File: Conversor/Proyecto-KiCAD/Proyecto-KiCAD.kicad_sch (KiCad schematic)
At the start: 6 parts

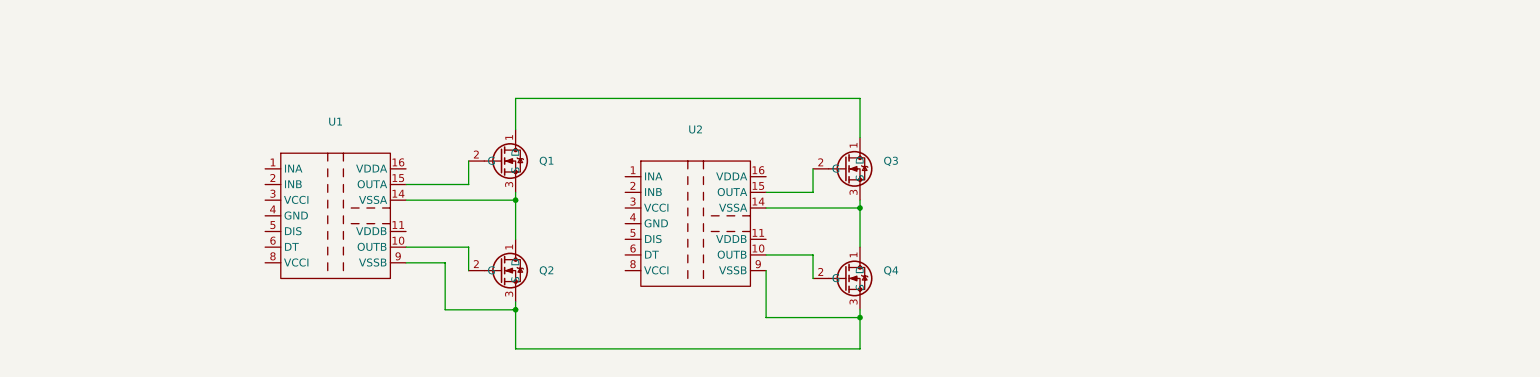
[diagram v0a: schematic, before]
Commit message: Comenzar el diseño de la plaqueta en KiCAD
- Empece a ver el diseño de los drivers para los MOSFETs
- Agregue la datasheet de la fuente aislada TRACO
- Hay que leer la nota de aplicacion para el diseño del circuito de bootstrap a la salida y elegir Cboot, Rboot y Dboot
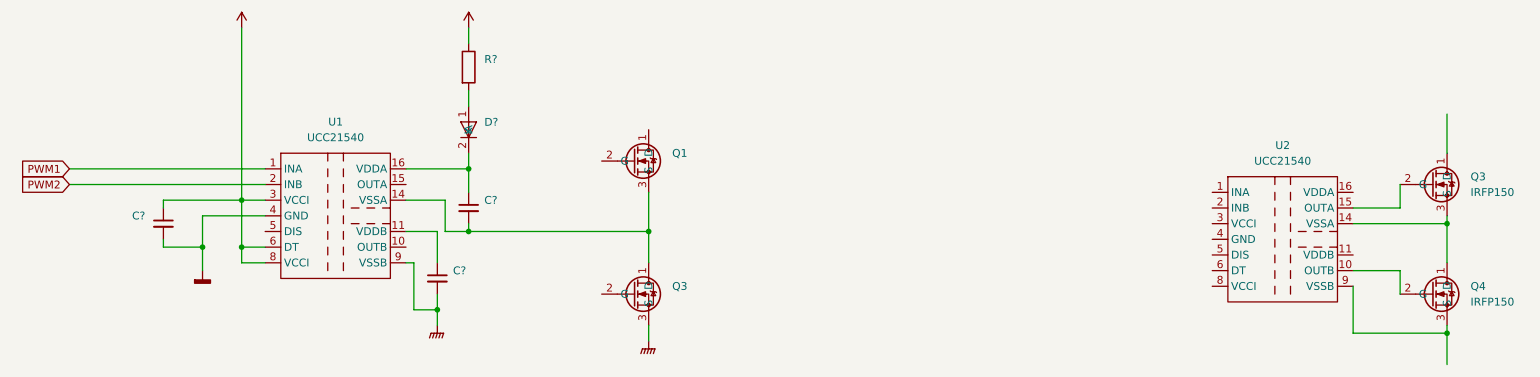
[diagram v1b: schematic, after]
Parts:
- removed Q2: (no value), symbol Componentes proyecto:IRFP150
- added C? (x3): (no value), symbol Device:C_Small
- added D?: (no value), symbol Componentes proyecto:MUR160
- added Q3: (no value), symbol Componentes proyecto:IRFP150
- added R?: (no value), symbol Device:R
- Q3, Q4: value (none) -> IRFP150; footprint (none) -> Package_TO_SOT_THT:TO-247-3_Horizontal_TabDown
- U1, U2: value (none) -> UCC21540; footprint (none) -> Package_SO:SOIC-16W_7.5x10.3mm_P1.27mm
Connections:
- net at Q1.3 (S), U1.14 (VSSA): now also C?.2, Q3.1 (D)
- net at Q4.3 (S), U2.9 (VSSB): no longer U1.9 (VSSB)
- net PWM1: now reaches U1.1 (INA)
- net at U1.11 (VDDB): now also C?.1
- net at Q1.2 (G): no longer U1.15 (OUTA)
- net at U1.16 (VDDA): now also C?.1, D?.2 (K)
- net PWM2: now reaches U1.2 (INB)
- net +5V: now reaches U1.3 (VCCI)
- net +5V: now also U1.6 (DT), U1.8 (VCCI), C?.1
- net GNDD: now reaches U1.4 (GND)
- net GNDD: now also C?.2
- net at Q1.1 (D): no longer Q3.1 (D)
- new net: D?.1 (A), R?.2
- new net +15V: R?.1
- new net GNDPWR: C?.2, Q3.3 (S), U1.9 (VSSB)
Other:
- moved on the sheet: Q3, Q4, U2

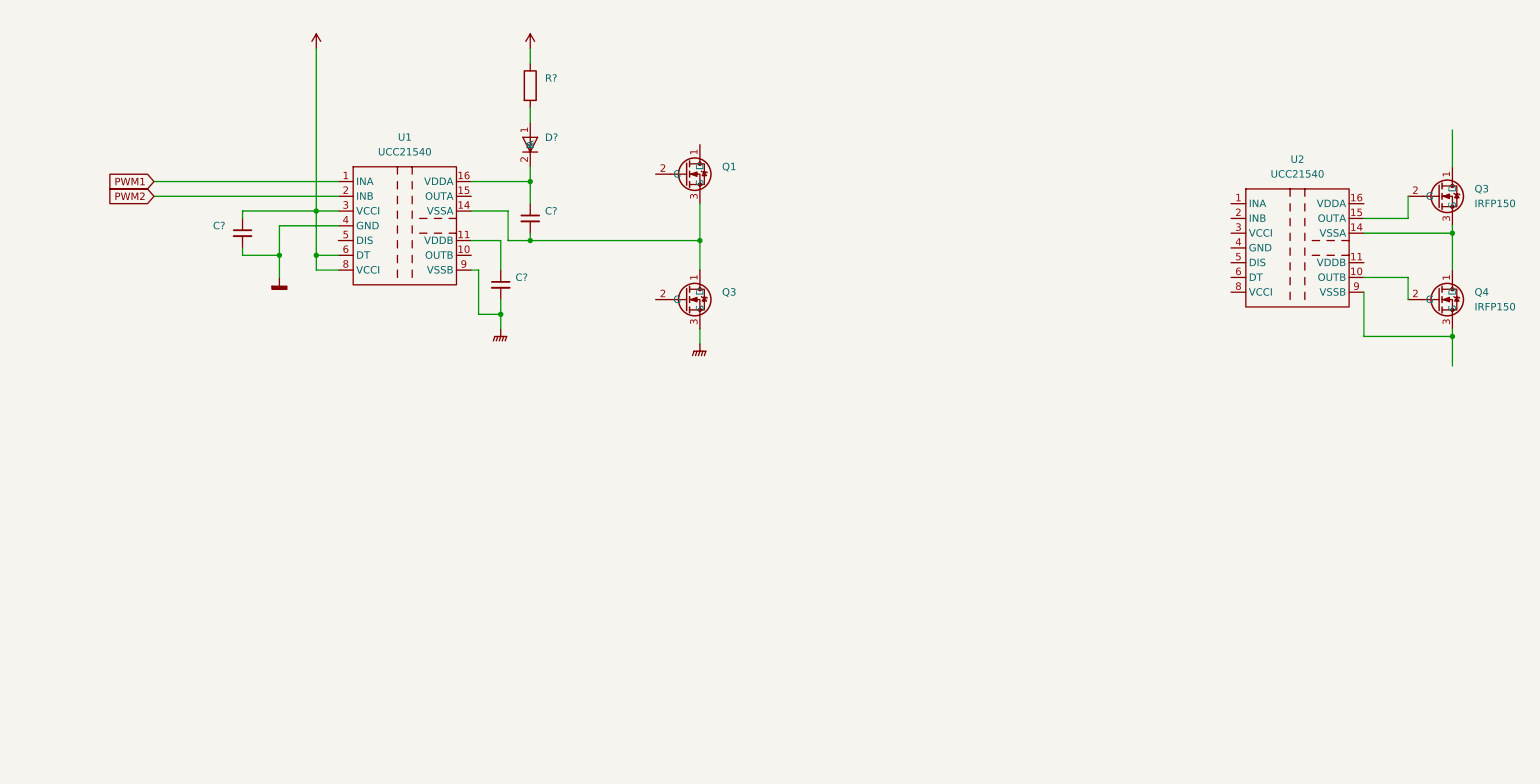
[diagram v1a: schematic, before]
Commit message: Completados (preliminarmente) los circuitos de los drivers
-Todos los componentes puestos y conectados en el esquematico (valores preliminares).
-Agregadas un par de datasheets de diodos del circuito del driver.
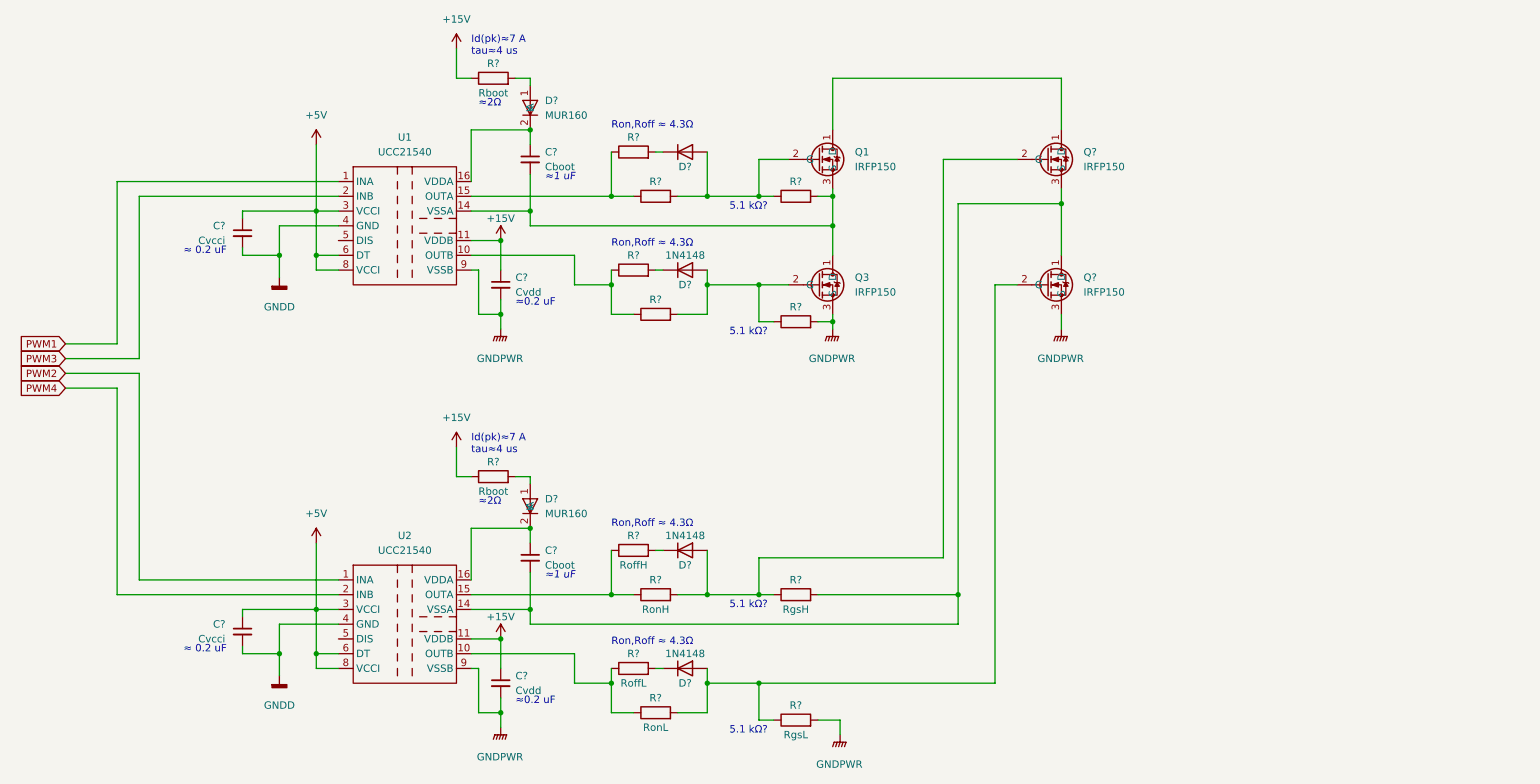
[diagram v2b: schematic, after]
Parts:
- removed Q3, Q4: IRFP150, Package_TO_SOT_THT:TO-247-3_Horizontal_TabDown, symbol Componentes proyecto:IRFP150
- added C?: Cvcci, symbol Device:C_Small
- added C?: Cboot, symbol Device:C_Small
- added C?: Cvdd, symbol Device:C_Small
- added D?: MUR160, symbol Componentes proyecto:MUR160
- added D?: (no value), symbol Diode:1N4148
- added D? (x3): 1N4148, Diode_THT:D_DO-35_SOD27_P7.62mm_Horizontal, symbol Diode:1N4148
- added Q? (x2): IRFP150, symbol Componentes proyecto:IRFP150
- added R?: RonL, symbol Device:R
- added R?: Rboot, symbol Device:R
- added R? (x6): (no value), symbol Device:R
- added R?: RgsH, symbol Device:R
- added R?: RoffL, symbol Device:R
- added R?: RgsL, symbol Device:R
- added R?: RonH, symbol Device:R
- added R?: RoffH, symbol Device:R
- C?: value (none) -> Cvdd
- C?: value (none) -> Cboot
- C?: value (none) -> Cvcci
- D?: value (none) -> MUR160
- Q1, Q3: value (none) -> IRFP150
- R?: value (none) -> Rboot
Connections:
- net +15V: now also C?.1, U1.11 (VDDB), U2.11 (VDDB), C?.1, R?.1
- net +5V: now also U2.3 (VCCI), U2.6 (DT), U2.8 (VCCI), C?.1
- net GNDD: now also U2.4 (GND), C?.2
- net GNDPWR: now also U2.9 (VSSB), C?.2, Q?.3 (S), R?.2, R?.2
- net PWM2: now also U2.1 (INA); no longer U1.2 (INB)
- net at Q1.1 (D): now also Q?.1 (D)
- net at Q1.2 (G): now also D?.2 (A), R?.1, R?.2
- net at C?.2, Q1.3 (S), Q3.1 (D)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: now also R?.2
- net at U1.10 (OUTB): now also R?.1, R?.1
- net at U1.15 (OUTA): now also R?.1, R?.1
- net at U2.10 (OUTB): now also R?.1, R?.1
- net at U2.14 (VSSA): now also C?.2, Q?.1 (D), Q?.3 (S), R?.2
- net at U2.15 (OUTA): now also R?.1, R?.1
- net at U2.16 (VDDA): now also C?.1, D?.2 (K)
- net PWM4: now reaches U2.2 (INB)
- net at Q3.2 (G): now also D?.2 (A), R?.1, R?.2
- new net: D?.1 (A), R?.2
- new net: D?.1 (K), R?.2 (x4)
- new net: D?.2 (A), Q?.2 (G), R?.1, R?.2 (x2)
- new net PWM3: U1.2 (INB)
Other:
- note added: "5.1 kΩ?"
- note added: "Id(pk)≈7 A tau≈4 us"
- note added: "Ron,Roff ≈ 4.3Ω"
- note added: "≈ 0.2 uF"
- note added: "≈0.2 uF"
- note added: "≈1 uF"
- note added: "≈2Ω"
- moved on the sheet: C?, D?, Q1, Q3, R?

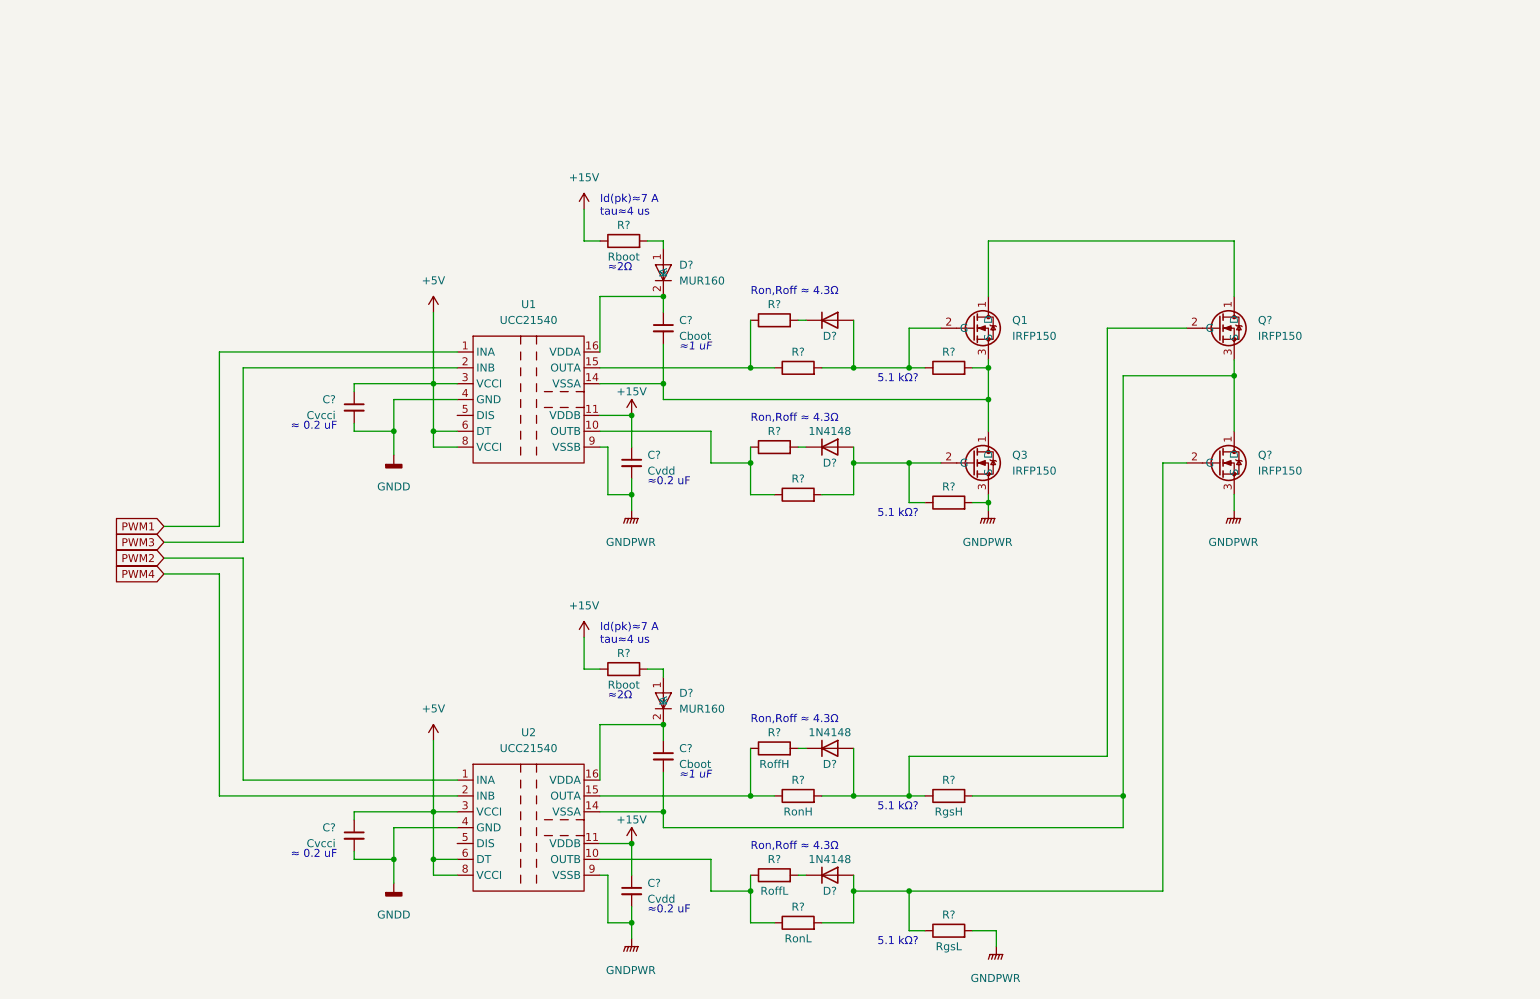
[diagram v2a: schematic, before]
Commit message: Continuar con el esquematico del conversor
-Completada el lado del primario + emprolijado un poco
-Hay que ver los diodos del secundario, porque los MUR1640CT son catodo comun y requeriria alguno de anodo comun para la parte de abajo del puente.
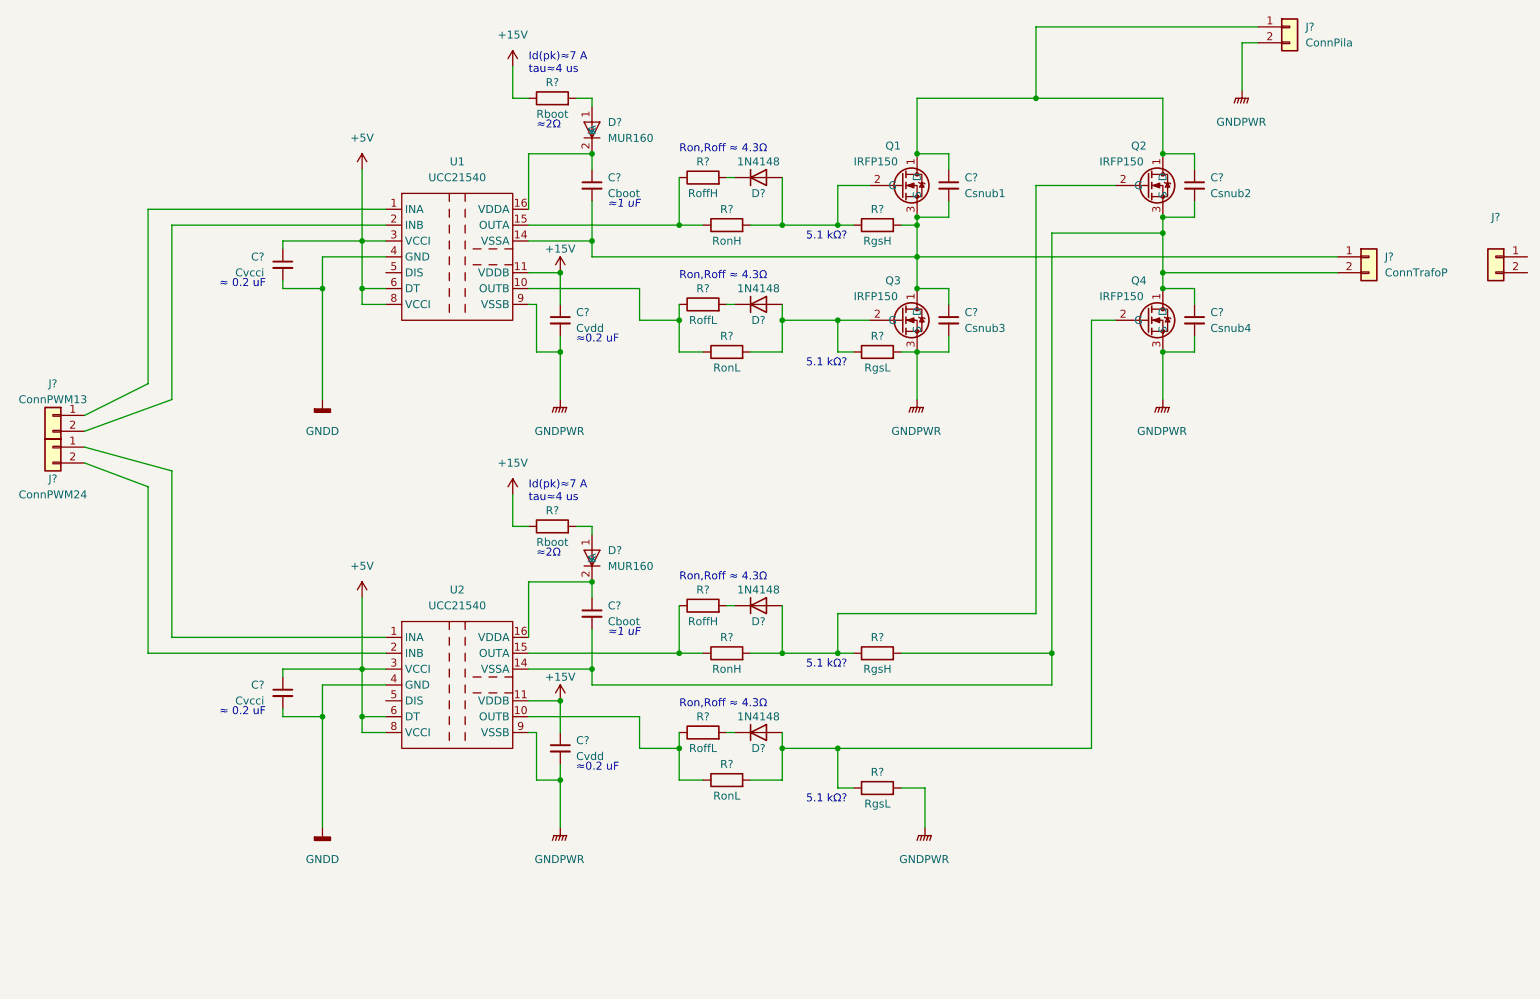
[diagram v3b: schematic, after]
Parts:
- added C?: Csnub4, symbol Device:C_Small
- added C?: Csnub2, symbol Device:C_Small
- added C?: Csnub1, symbol Device:C_Small
- added C?: Csnub3, symbol Device:C_Small
- added J?: ConnPila, symbol Connector_Generic:Conn_01x02
- added J?: ConnPWM24, symbol Connector_Generic:Conn_01x02
- added J?: (no value), symbol Connector_Generic:Conn_01x02
- added J?: ConnPWM13, symbol Connector_Generic:Conn_01x02
- added J?: ConnTrafoP, symbol Connector_Generic:Conn_01x02
- D?: value (none) -> 1N4148; footprint (none) -> Diode_THT:D_DO-35_SOD27_P7.62mm_Horizontal
- R?: value (none) -> RoffH
- R?: value (none) -> RonH
- R?: value (none) -> RonL
- R?: value (none) -> RgsL
- R?: value (none) -> RoffL
- R?: value (none) -> RgsH
- gave numbers to parts that had none: 2
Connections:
- net GNDPWR: now also C?.2, C?.2, J?.2 (Pin_2)
- net at C?.2, Q2.3 (S), Q4.1 (D)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: now also C?.1, C?.2, J?.2 (Pin_2)
- net at Q1.1 (D), Q2.1 (D): now also C?.1, C?.1, J?.1 (Pin_1)
- net at C?.2, Q1.3 (S), Q3.1 (D)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: now also C?.1, C?.2, J?.1 (Pin_1)
- net PWM1: no longer names the net of U1.1 (INA)
- net PWM1: now also J?.1 (Pin_1)
- net PWM2: no longer names the net of U2.1 (INA)
- net PWM2: now also J?.1 (Pin_1)
- net PWM3: no longer names the net of U1.2 (INB)
- net PWM3: now also J?.2 (Pin_2)
- net PWM4: no longer names the net of U2.2 (INB)
- net PWM4: now also J?.2 (Pin_2)
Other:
- moved on the sheet: C?, D?, Q1, Q2, Q3, Q4, R?, U1, U2
